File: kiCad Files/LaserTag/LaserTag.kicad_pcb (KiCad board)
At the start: 2 copper layers, 50.8 x 25.4 mm, 9 parts, among them J1 Conn_01x01_Male, J2 Conn_01x02_Male, U1 LM741

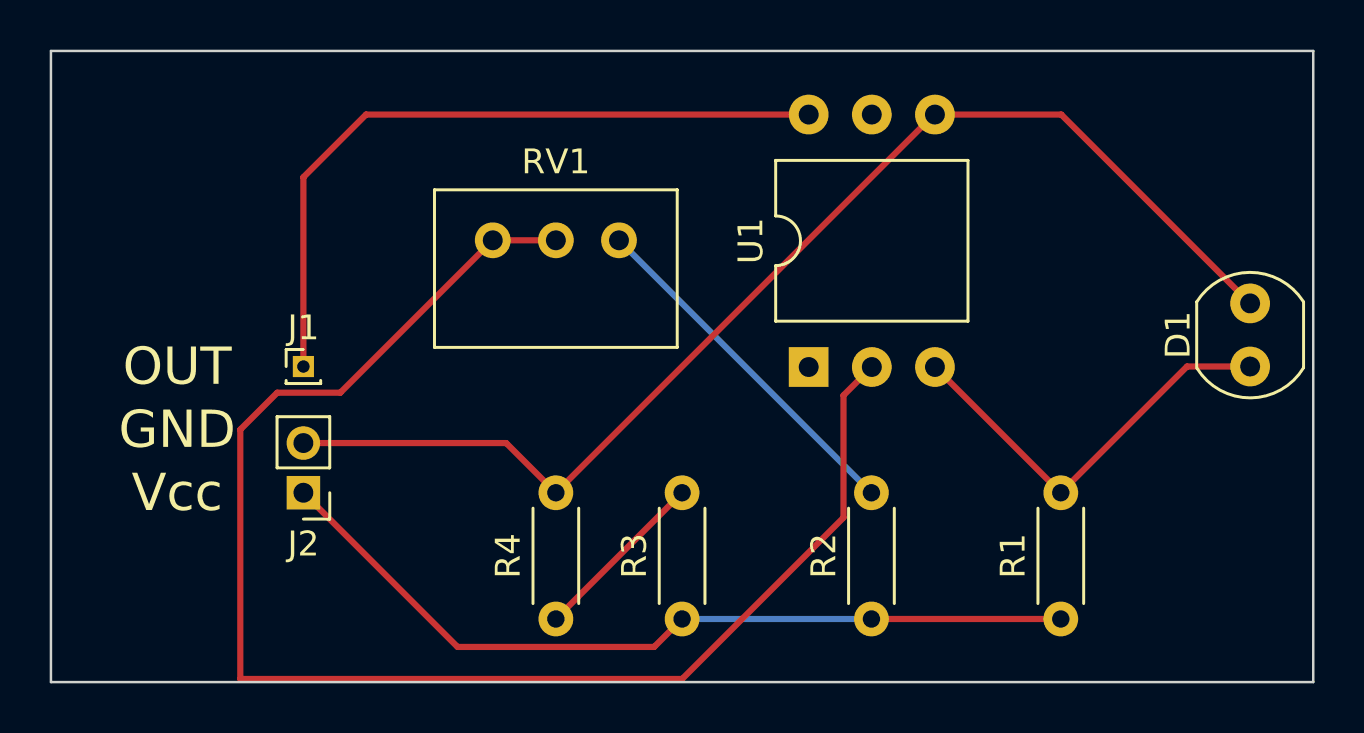
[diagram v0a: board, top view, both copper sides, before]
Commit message: transmitter Circuit created + receiver resized
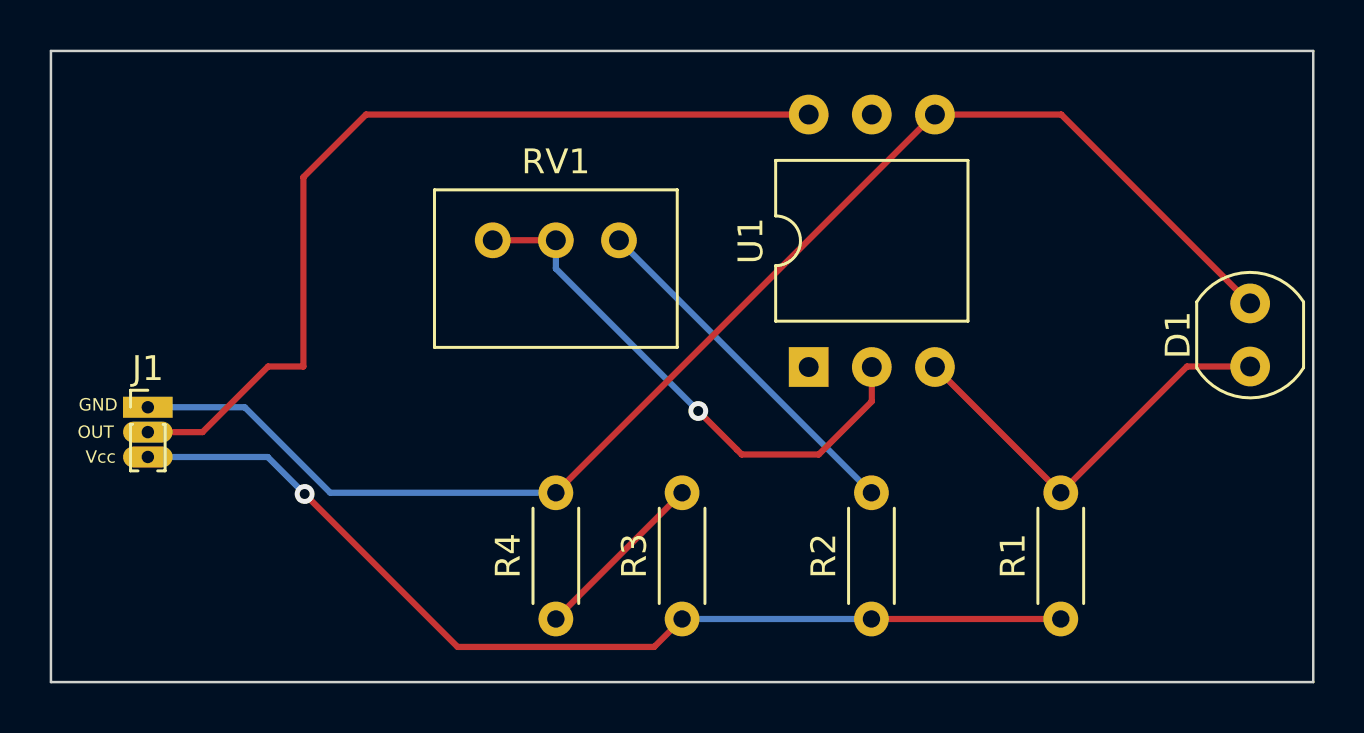
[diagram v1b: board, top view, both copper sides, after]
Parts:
- removed J2: Conn_01x02_Male, Connector_PinHeader_2.00mm:PinHeader_1x02_P2.00mm_Vertical
- J1: value Conn_01x01_Male -> Conn_01x03; footprint Connector_PinHeader_1.00mm:PinHeader_1x01_P1.00mm_Vertical -> Connector_PinHeader_1.00mm:PinHeader_1x03_P1.00mm_Vertical
- moved J1 6.47 mm to (105.5, 75.3)
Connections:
- net Net-(R3-Pad2) renamed +5v
- J1 pad 1: Net-(U1-Pad6) -> GND
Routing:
- net Net-(RV1-Pad2): track 59.4 -> 21.9 mm, vias 0 -> 1
- net Net-(U1-Pad6): track 29.0 -> 36.4 mm
- net +9V: track 33.5 -> 40.4 mm, vias 0 -> 1
- net GND: track 48.4 -> 55.2 mm
